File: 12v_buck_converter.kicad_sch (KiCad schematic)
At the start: 18 parts, among them IC1 TPS56A37RPAR

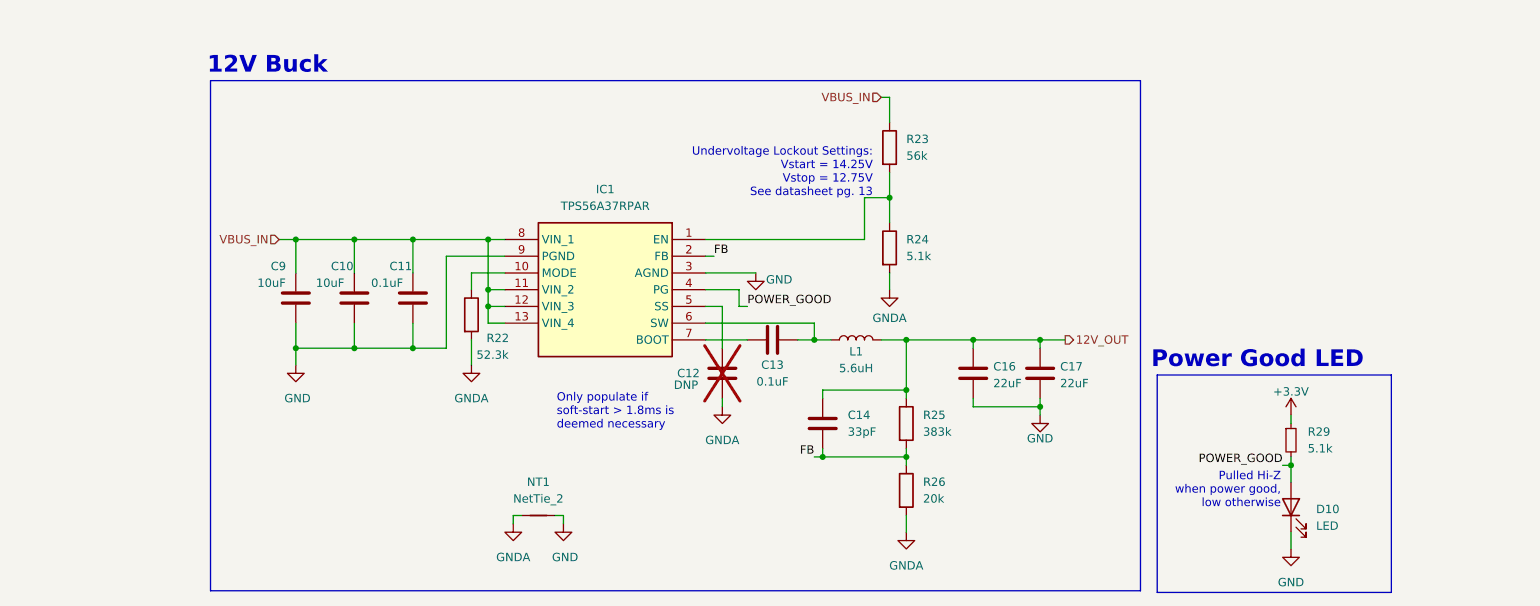
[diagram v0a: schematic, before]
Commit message: Added ideal diode controller & mosfet for 12V buck power protection
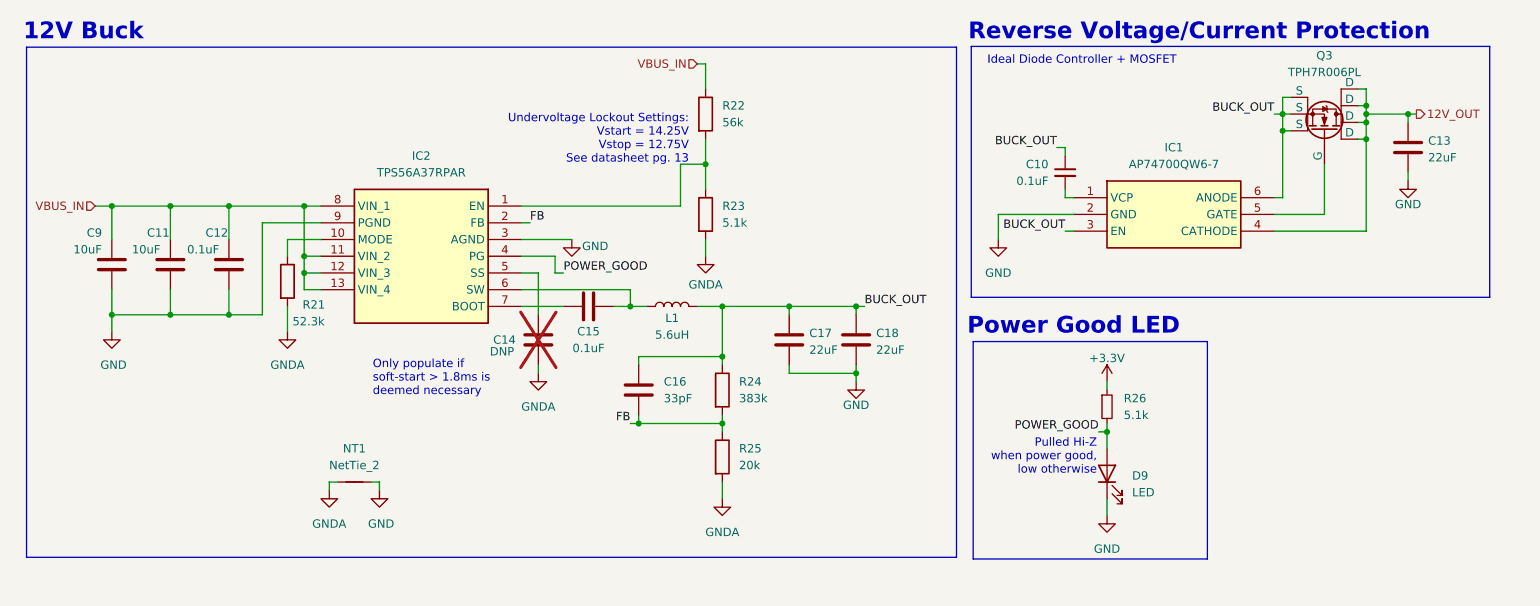
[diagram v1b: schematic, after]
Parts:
- added C10: 0.1uF, Capacitor_SMD:C_0805_2012Metric, symbol Device:C_Small
- added C13: 22uF, Capacitor_SMD:C_1210_3225Metric, symbol Device:C
- added IC1: AP74700QW6-7, SOT95P285X140-6N, symbol utsvt-power-regulators:AP74700QW6-7
- added Q3: TPH7R006PL, symbol Simulation_SPICE:NMOS
- renumbered C10 to C11, C11 to C12, C12 to C14, C13 to C15, C14 to C16, C16 to C17, C17 to C18, D10 to D9, IC1 to IC2, R22 to R21, R23 to R22, R24 to R23, R25 to R24, R26 to R25, R29 to R26
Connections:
- net 12V_OUT: now also C13.1, IC1.4 (CATHODE), Q3.5 (D), Q3.6 (D), Q3.7 (D), Q3.8 (D); no longer C16.1, C17.1, C18.1, L1.2, R24.1
- net GND: now also C13.2, IC1.2 (GND)
- new net: C10.2, IC1.1 (VCP)
- new net: IC1.5 (GATE), Q3.4 (G)
- new net BUCK_OUT: C10.1, C16.1, C17.1, C18.1, IC1.3 (EN), IC1.6 (ANODE), L1.2, Q3.1 (S), Q3.2 (S), Q3.3 (S), R24.1
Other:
- note added: "Ideal Diode Controller + MOSFET"
- note added: "Reverse Voltage/Current Protection"
- moved on the sheet: C11, C12, C14, C15, C16, C17, C18, C9, D9, IC2, L1, NT1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

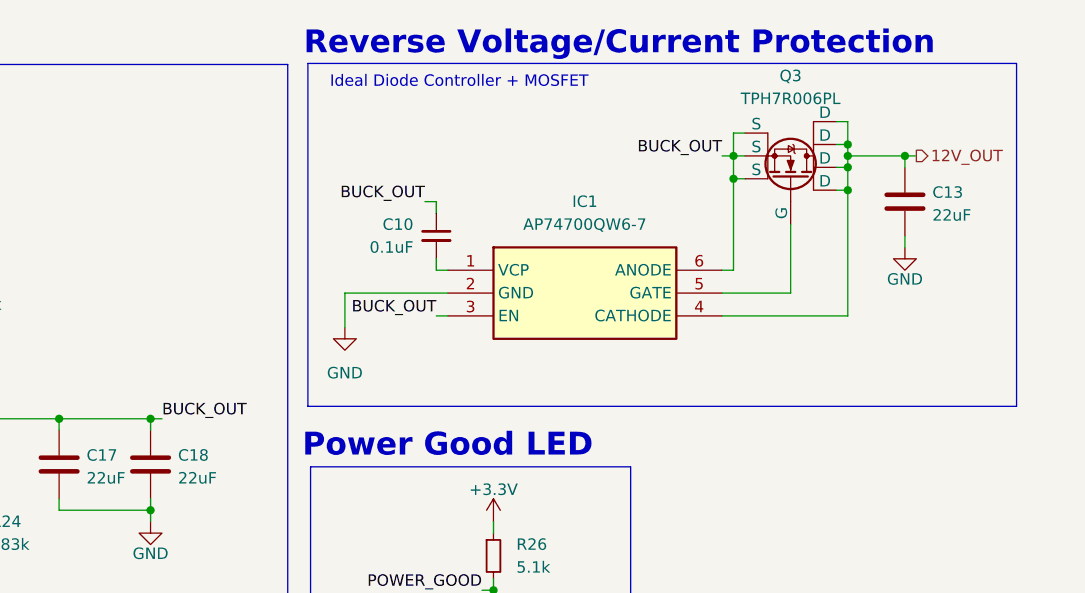
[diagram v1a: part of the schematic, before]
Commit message: removed 12v output protection since buck already has OV
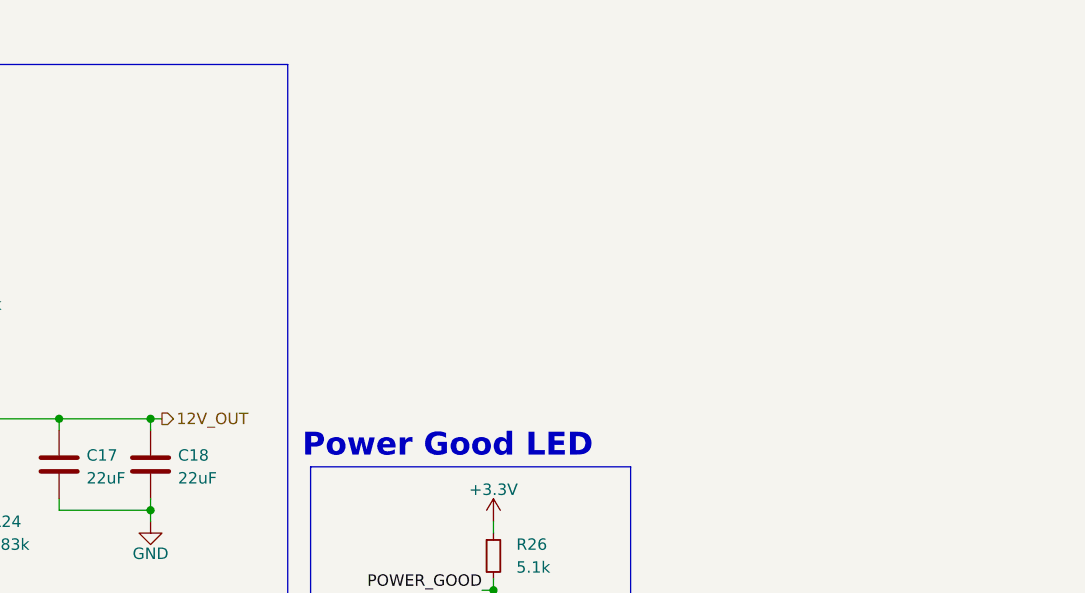
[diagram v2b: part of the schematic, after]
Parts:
- removed C10: 0.1uF, Capacitor_SMD:C_0805_2012Metric, symbol Device:C_Small
- removed C13: 22uF, Capacitor_SMD:C_1210_3225Metric, symbol Device:C
- removed IC1: AP74700QW6-7, SOT95P285X140-6N, symbol utsvt-power-regulators:AP74700QW6-7
- removed Q3: TPH7R006PL, symbol Simulation_SPICE:NMOS
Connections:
- net BUCK_OUT is gone; now on net 12V_OUT: C16.1, C17.1, C18.1, L1.2, R24.1
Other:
- note removed: "Ideal Diode Controller + MOSFET"
- note removed: "Reverse Voltage/Current Protection"

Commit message: started routing
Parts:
- C11, C9: footprint Capacitor_SMD:C_2220_5750Metric -> Capacitor_SMD:C_0805_2012Metric; Manufacturer_Name KEMET -> Murata; Mouser Part Number C2220C106M5RACTU -> GRM21BR61H106KE43L
- C17, C18: footprint Capacitor_SMD:C_1210_3225Metric -> Capacitor_SMD:C_0805_2012Metric; Manufacturer_Name Taiyo Yuden -> TDK; Mouser Part Number GMK325BJ226MM-P -> C2012X5R1V226M125AC
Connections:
- net SW: now reaches C15.2, IC2.6 (SW), L1.1
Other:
- moved on the sheet: C11, C12, C14, C15, C16, C17, C18, C9, D9, IC2, L1, NT1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

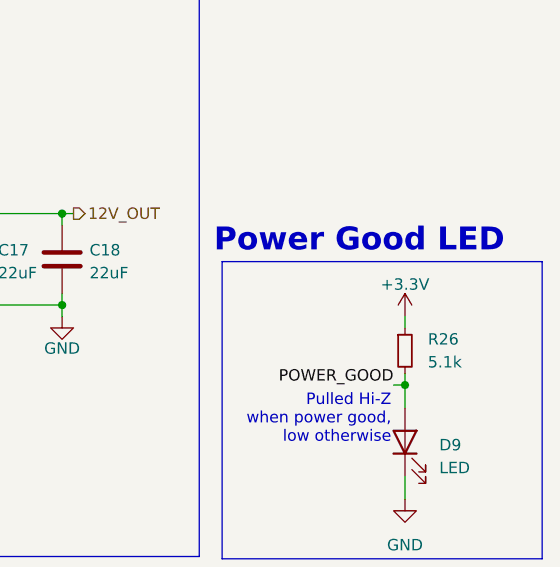
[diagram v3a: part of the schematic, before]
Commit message: redid cypd layout, halfway through 12v buck layout
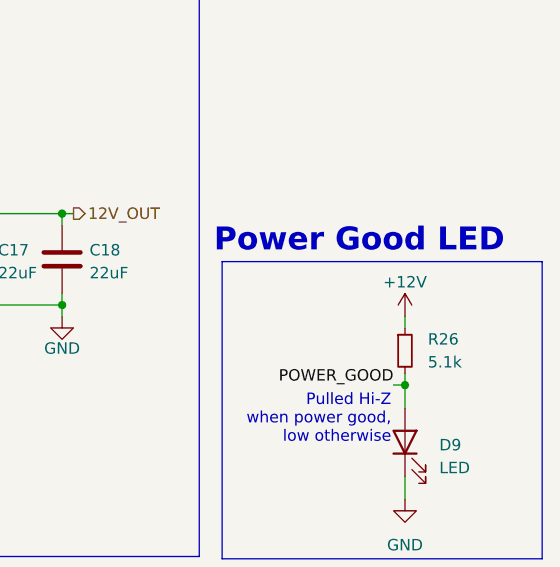
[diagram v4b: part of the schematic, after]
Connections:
- net +3.3V renamed +12V
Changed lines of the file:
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@@
 	)
 	(symbol
-		(lib_id "power:+3.3V")
+		(lib_id "power:+12V")
 		(at 228.6 107.95 0)
 		(unit 1)
@@
 		(on_board yes)
 		(dnp no)
-		(property "Reference" "#PWR059"
+		(property "Reference" "#PWR048"
 			(at 228.6 111.76 0)
 			(effects
@@
 			)
 		)
-		(property "Value" "+3.3V"
-			(at 228.6 104.394 0)
+		(property "Value" "+12V"
+			(at 228.6 104.14 0)
 			(effects
 				(font
@@
 			)
 		)
-		(property "Description" "Power symbol creates a global label with name \"+3.3V\""
+		(property "Description" "Power symbol creates a global label with name \"+12V\""
 			(at 228.6 107.95 0)
 			(effects
@@
 			(project ""
 				(path "/f58400c5-df4b-4929-8d2b-33c0fe23fcd9/01d27e83-9627-42d8-8cf9-628e44513f14"
-					(reference "#PWR059")
+					(reference "#PWR048")
 					(unit 1)
 				)

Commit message: big component layout moment
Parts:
- added TP14: 12V_UVLO, TestPoint:TestPoint_THTPad_1.0x1.0mm_Drill0.5mm, symbol Connector:TestPoint
- added TP16: 12V_SET, TestPoint:TestPoint_THTPad_1.0x1.0mm_Drill0.5mm, symbol Connector:TestPoint
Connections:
- net FB: now also TP16.1
- net at IC2.1 (EN), R22.2, R23.1: now also TP14.1
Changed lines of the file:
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@@
 	(wire
 		(pts
+			(xy 179.07 114.3) (xy 179.07 113.03)
+		)
+		(stroke
+			(width 0)
+			(type default)
+		)
+	)
+	(wire
+		(pts
 			(xy 109.22 91.44) (xy 106.68 91.44)
 		)
@@
 	(wire
 		(pts
+			(xy 170.18 114.3) (xy 179.07 114.3)
+		)
+		(stroke
+			(width 0)
+			(type default)
+		)
+	)
+	(wire
+		(pts
 			(xy 167.64 74.93) (xy 167.64 78.74)
 		)
@@
 	(wire
 		(pts
+			(xy 167.64 74.93) (xy 170.18 74.93)
+		)
+		(stroke
+			(width 0)
+			(type default)
+		)
+	)
+	(wire
+		(pts
 			(xy 109.22 86.36) (xy 104.14 86.36)
 		)
@@
 	)
 	(symbol
+		(lib_id "Connector:TestPoint")
+		(at 179.07 113.03 0)
+		(unit 1)
+		(exclude_from_sim no)
+		(in_bom yes)
+		(on_board yes)
+		(dnp no)
+		(property "Reference" "TP16"
+			(at 180.086 108.458 0)
+			(effects
+				(font
+					(size 1.27 1.27)
+				)
+				(justify left)
+			)
+		)
+		(property "Value" "12V_SET"
+			(at 180.086 110.998 0)
+			(effects
+				(font
+					(size 1.27 1.27)
+				)
+				(justify left)
+			)
+		)
+		(property "Footprint" "TestPoint:TestPoint_THTPad_1.0x1.0mm_Drill0.5mm"
+			(at 184.15 113.03 0)
+			(effects
+				(font
+					(size 1.27 1.27)
+				)
+				(hide yes)
+			)
+		)
+		(property "Datasheet" "~"
+			(at 184.15 113.03 0)
+			(effects
+				(font
+					(size 1.27 1.27)
+				)
+				(hide yes)
+			)
+		)
+		(property "Description" "test point"
+			(at 179.07 113.03 0)
+			(effects
+				(font
+					(size 1.27 1.27)
+				)
+				(hide yes)
+			)
+		)
+		(pin "1"
+		)
+		(instances
+			(project "USBCPowerPCB"
+				(path "/f58400c5-df4b-4929-8d2b-33c0fe23fcd9/01d27e83-9627-42d8-8cf9-628e44513f14"
+					(reference "TP16")
+					(unit 1)
+				)
+			)
+		)
+	)
+	(symbol
 		(lib_id "Device:C")
 		(at 77.47 90.17 0)
@@
 					(unit 1)
 				)
+			)
+		)
+	)
+	(symbol
+		(lib_id "Connector:TestPoint")
+		(at 170.18 74.93 0)
+		(unit 1)
+		(exclude_from_sim no)
+		(in_bom yes)
+		(on_board yes)
+		(dnp no)
+		(fields_autoplaced yes)
+		(property "Reference" "TP14"
+			(at 172.72 70.3579 0)
+			(effects
+				(font
+					(size 1.27 1.27)
+				)
+				(justify left)
+			)
+		)
+		(property "Value" "12V_UVLO"
+			(at 172.72 72.8979 0)
+			(effects
+				(font
+					(size 1.27 1.27)
+				)
+				(justify left)
+			)
+		)
+		(property "Footprint" "TestPoint:TestPoint_THTPad_1.0x1.0mm_Drill0.5mm"
+			(at 175.26 74.93 0)
+			(effects
+				(font
+					(size 1.27 1.27)
+				)
+				(hide yes)
+			)
+		)
+		(property "Datasheet" "~"
+			(at 175.26 74.93 0)
+			(effects
+				(font
+					(size 1.27 1.27)
+				)
+				(hide yes)
+			)
+		)
+		(property "Description" "test point"
+			(at 170.18 74.93 0)
+			(effects
+				(font
+					(size 1.27 1.27)
+				)
+				(hide yes)
+			)
+		)
+		(pin "1"
+		)
+		(instances
+			(project ""
+				(path "/f58400c5-df4b-4929-8d2b-33c0fe23fcd9/01d27e83-9627-42d8-8cf9-628e44513f14"
+					(reference "TP14")
+					(unit 1)
+				)

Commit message: addressed some review comments from my 🐐 champers fu
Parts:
- L1: footprint UTSVT_Passive:INDPM110100X400N -> Inductor_SMD:L_Bourns_SRP1038C_10.0x10.0mm
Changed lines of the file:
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@@
 			)
 		)
-		(property "Footprint" "UTSVT_Passive:INDPM110100X400N"
+		(property "Footprint" "Inductor_SMD:L_Bourns_SRP1038C_10.0x10.0mm"
 			(at 162.56 96.52 0)
 			(effects

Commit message: i am jesus christ in the flesh.
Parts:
- C11, C9: Mouser Part Number GRM21BR61H106KE43L -> (none); P/N (none) -> GRM21BR61H106KE43L
- C12, C15: Mouser Part Number C0805C104M5RACTU -> (none); P/N (none) -> C0805C104M5RACTU
- C16: Mouser Part Number C0805C330K5RACTU -> (none); P/N (none) -> C0805C330K5RACTU
- C17, C18: Mouser Part Number C2012X5R1V226M125AC -> (none); P/N (none) -> C2012X5R1V226M125AC
- D9: Mouser Part Number 604-APTD2012LCGCK -> (none); P/N (none) -> APTD2012LCGCK
- IC2: Mouser Part Number 595-TPS56A37RPAR -> (none); P/N (none) -> TPS56A37RPAR
- L1: Mouser Part Number SRP1038CC-5R6M -> (none); P/N (none) -> SRP1038CC-5R6M
- R21: Mouser Part Number CRCW080552K3FKEAC -> (none); P/N (none) -> CRCW080552K3FKEA
- R22: Mouser Part Number CRCW080556K0FKEAC -> (none); P/N (none) -> CRCW080556K0FKEAC
- R23, R26: Mouser Part Number CRCW08055K10FKEAC -> (none); P/N (none) -> CRCW08055K10FKEAC
- R24: Mouser Part Number CRCW0805383KFKEAC -> (none); P/N (none) -> CRCW0805383KFKEA
- R25: Mouser Part Number CRCW080520K0FKEAC -> (none); P/N (none) -> CRCW080520K0FKEAC
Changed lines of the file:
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@@
 			)
 		)
-		(property "Mouser Part Number" "C2012X5R1V226M125AC"
+		(property "Mouser Part Number" ""
 			(at 180.34 101.6 0)
 			(effects
@@
 			)
 		)
+		(property "P/N" "C2012X5R1V226M125AC"
+			(at 180.34 101.6 0)
+			(effects
+				(font
+					(size 1.27 1.27)
+				)
+				(hide yes)
+			)
+		)
 		(pin "1"
 		)
@@
 			)
 		)
-		(property "Mouser Part Number" "SRP1038CC-5R6M"
+		(property "Mouser Part Number" ""
 			(at 162.56 96.52 0)
 			(effects
@@
 			)
 		)
+		(property "P/N" "SRP1038CC-5R6M"
+			(at 162.56 96.52 0)
+			(effects
+				(font
+					(size 1.27 1.27)
+				)
+				(hide yes)
+			)
+		)
 		(pin "1"
 		)
@@
 			)
 		)
-		(property "Mouser Part Number" "CRCW0805383KFKEAC"
+		(property "Mouser Part Number" ""
 			(at 170.18 109.22 0)
 			(effects
@@
 			)
 		)
+		(property "P/N" "CRCW0805383KFKEA"
+			(at 170.18 109.22 0)
+			(effects
+				(font
+					(size 1.27 1.27)
+				)
+				(hide yes)
+			)
+		)
 		(pin "1"
 		)
@@
 			)
 		)
-		(property "Mouser Part Number" "C0805C330K5RACTU"
+		(property "Mouser Part Number" ""
 			(at 157.48 109.22 0)
 			(effects
@@
 			)
 		)
+		(property "P/N" "C0805C330K5RACTU"
+			(at 157.48 109.22 0)
+			(effects
+				(font
+					(size 1.27 1.27)
+				)
+				(hide yes)
+			)
+		)
 		(pin "1"
 		)
@@
 			)
 		)
-		(property "Mouser Part Number" "CRCW080556K0FKEAC"
+		(property "Mouser Part Number" ""
 			(at 167.64 67.31 0)
 			(effects
@@
 			)
 		)
+		(property "P/N" "CRCW080556K0FKEAC"
+			(at 167.64 67.31 0)
+			(effects
+				(font
+					(size 1.27 1.27)
+				)
+				(hide yes)
+			)
+		)
 		(pin "1"
 		)
@@
 			)
 		)
-		(property "Mouser Part Number" "CRCW080552K3FKEAC"
+		(property "Mouser Part Number" ""
 			(at 104.14 92.71 0)
 			(effects
@@
 			)
 		)
+		(property "P/N" "CRCW080552K3FKEA"
+			(at 104.14 92.71 0)
+			(effects
+				(font
+					(size 1.27 1.27)
+				)
+				(hide yes)
+			)
+		)
 		(pin "1"
 		)
@@
 			)
 		)
-		(property "Mouser Part Number" "C0805C104M5RACTU"
+		(property "Mouser Part Number" ""
 			(at 149.86 96.52 0)
 			(effects
@@
 			)
 		)
+		(property "P/N" "C0805C104M5RACTU"
+			(at 149.86 96.52 0)
+			(effects
+				(font
+					(size 1.27 1.27)
+				)
+				(hide yes)
+			)
+		)
 		(pin "1"
 		)
@@
 			)
 		)
-		(property "Mouser Part Number" "C2012X5R1V226M125AC"
+		(property "Mouser Part Number" ""
 			(at 190.5 101.6 0)
 			(effects
@@
 			)
 		)
+		(property "P/N" "C2012X5R1V226M125AC"
+			(at 190.5 101.6 0)
+			(effects
+				(font
+					(size 1.27 1.27)
+				)
+				(hide yes)
+			)
+		)
 		(pin "1"
 		)
@@
 			)
 		)
-		(property "Mouser Part Number" "CRCW08055K10FKEAC "
+		(property "Mouser Part Number" ""
 			(at 167.64 82.55 0)
 			(effects
@@
 			)
 		)
+		(property "P/N" "CRCW08055K10FKEAC "
+			(at 167.64 82.55 0)
+			(effects
+				(font
+					(size 1.27 1.27)
+				)
+				(hide yes)
+			)
+		)
 		(pin "1"
 		)
@@
 			)
 		)
-		(property "Mouser Part Number" " GRM21BR61H106KE43L "
+		(property "Mouser Part Number" ""
 			(at 86.36 90.17 0)
 			(effects
@@
 			)
 		)
+		(property "P/N" " GRM21BR61H106KE43L "
+			(at 86.36 90.17 0)
+			(effects
+				(font
+					(size 1.27 1.27)
+				)
+				(hide yes)
+			)
+		)
 		(pin "1"
 		)
@@
 			)
 		)
-		(property "Mouser Part Number" "604-APTD2012LCGCK"
+		(property "Mouser Part Number" ""
 			(at 228.6 121.92 0)
 			(effects
@@
 			)
 		)
+		(property "P/N" "APTD2012LCGCK"
+			(at 228.6 121.92 0)
+			(effects
+				(font
+					(size 1.27 1.27)
+				)
+				(hide yes)
+			)
+		)
 		(pin "2"
 		)
@@
 			)
 		)
-		(property "Mouser Part Number" "CRCW080520K0FKEAC"
+		(property "Mouser Part Number" ""
 			(at 170.18 119.38 0)
 			(effects
@@
 			)
 		)
+		(property "P/N" "CRCW080520K0FKEAC"
+			(at 170.18 119.38 0)
+			(effects
+				(font
+					(size 1.27 1.27)
+				)
+				(hide yes)
+			)
+		)
 		(pin "1"
 		)
@@
 			)
 		)
-		(property "Mouser Part Number" " GRM21BR61H106KE43L "
+		(property "Mouser Part Number" ""
 			(at 77.47 90.17 0)
 			(effects
@@
 			)
 		)
+		(property "P/N" " GRM21BR61H106KE43L "
+			(at 77.47 90.17 0)
+			(effects
+				(font
+					(size 1.27 1.27)
+				)
+				(hide yes)
+			)
+		)
 		(pin "1"
 		)
@@
 			)
 		)
-		(property "Mouser Part Number" "595-TPS56A37RPAR"
+		(property "Mouser Part Number" ""
 			(at 113.03 576.2 0)
 			(effects
@@
 			)
 		)
+		(property "P/N" "TPS56A37RPAR"
+			(at 139.7 81.28 0)
+			(effects
+				(font
+					(size 1.27 1.27)
+				)
+				(hide yes)
+			)
+		)
 		(pin "6"
 		)
@@
 			)
 		)
-		(property "Mouser Part Number" "C0805C104M5RACTU"
+		(property "Mouser Part Number" ""
 			(at 95.25 90.17 0)
 			(effects
@@
 			)
 		)
+		(property "P/N" "C0805C104M5RACTU"
+			(at 95.25 90.17 0)
+			(effects
+				(font
+					(size 1.27 1.27)
+				)
+				(hide yes)
+			)
+		)
 		(pin "1"
 		)
@@
 			)
 		)
-		(property "Mouser Part Number" "CRCW08055K10FKEAC "
+		(property "Mouser Part Number" ""
 			(at 228.6 111.76 0)
 			(effects
@@
 			(at 228.6 111.76 0)
 			(effects
+				(font
+					(size 1.27 1.27)
+				)
+				(hide yes)
+			)
+		)
+		(property "P/N" "CRCW08055K10FKEAC "
+			(at 228.6 111.76 0)
+			(effects
